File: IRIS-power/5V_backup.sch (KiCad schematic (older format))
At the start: 20 parts, among them Q61 IRLML6402, U61 LTC3110, U62 PCA9537

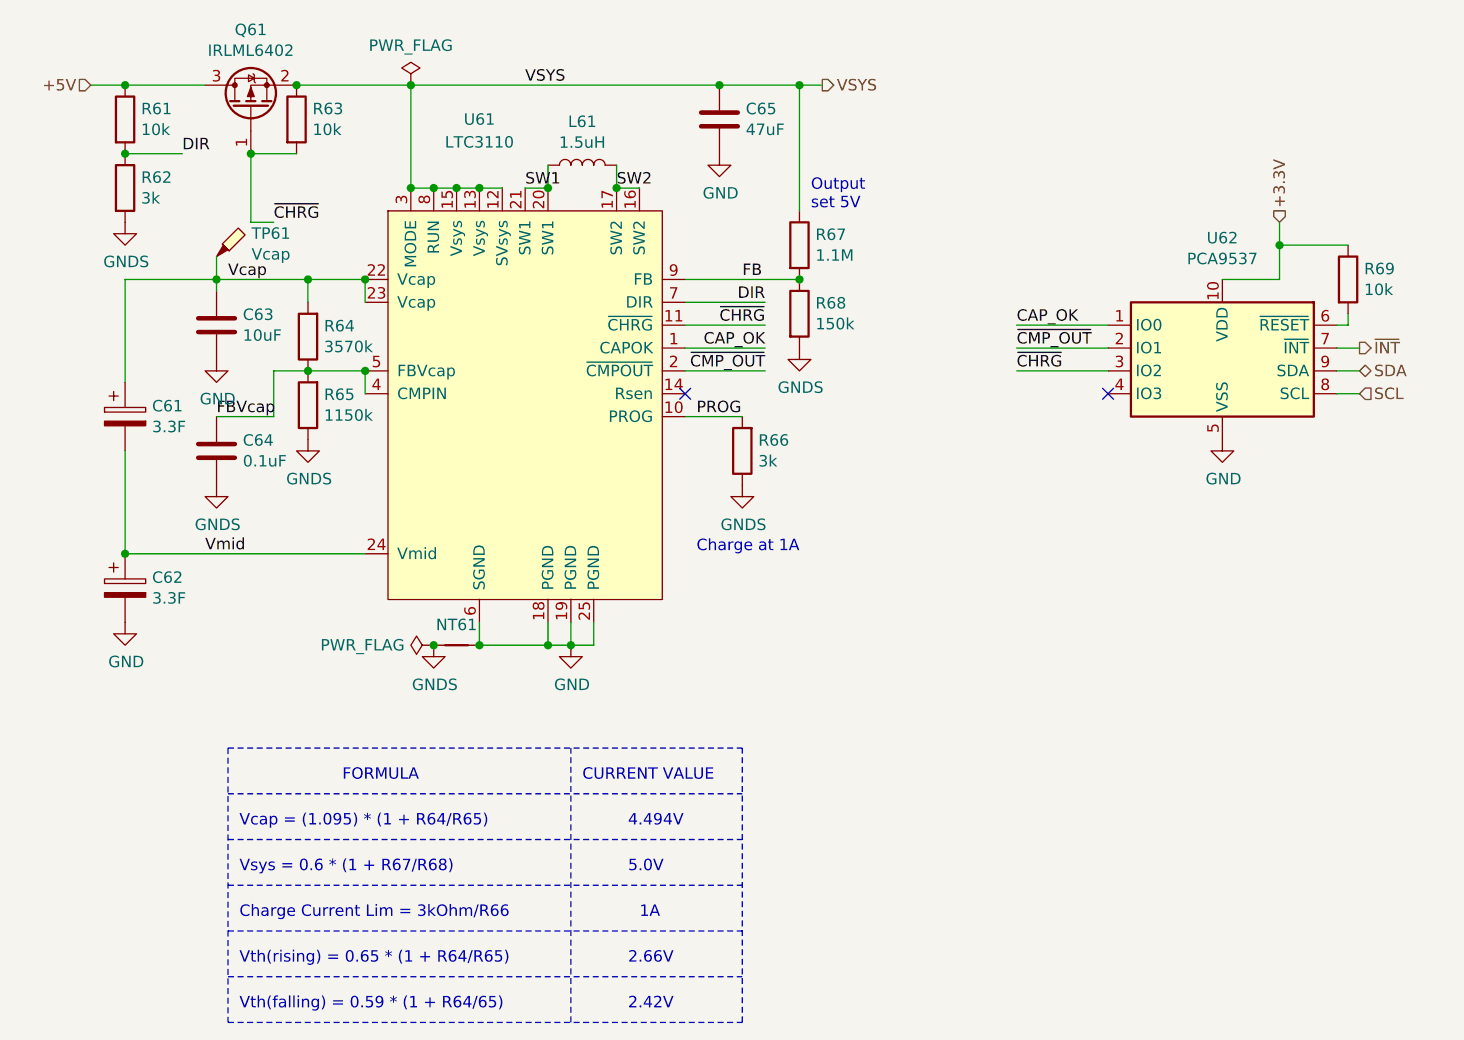
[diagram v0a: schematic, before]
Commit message: Adjusted silkscreen
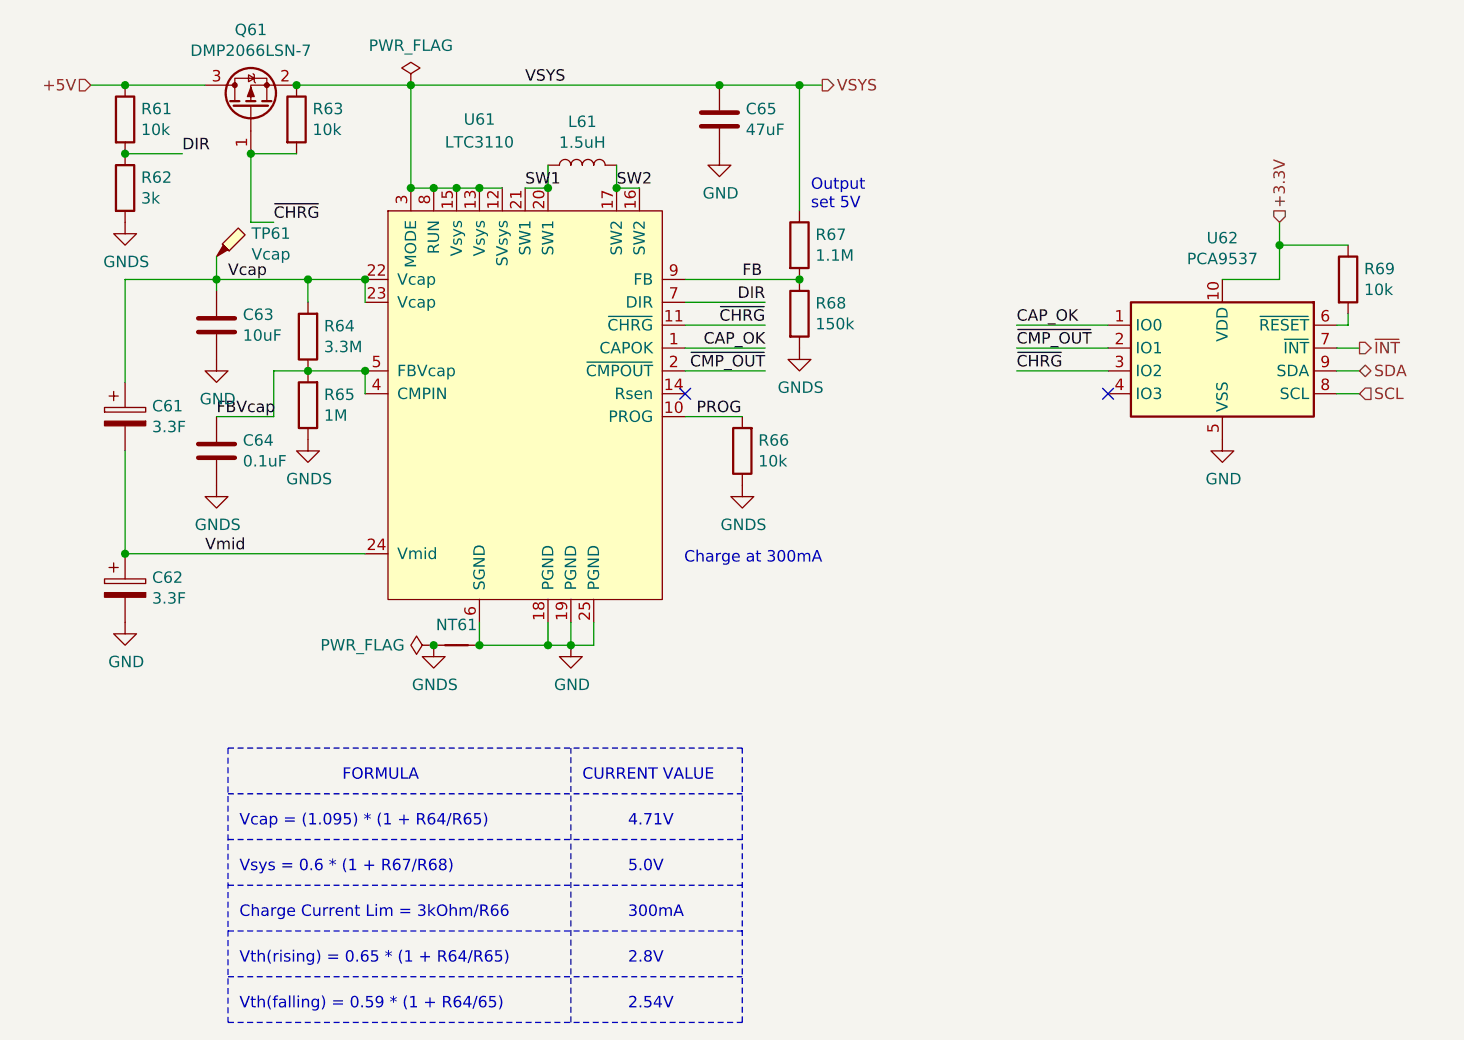
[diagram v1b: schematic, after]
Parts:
- Q61: value IRLML6402 -> DMP2066LSN-7; Digikey PN (none) -> DMP2066LSNDICT-ND
- R62: Digikey PN (none) -> RMCF0603FT3K00CT-ND
- R64: value 3570k -> 3.3M; Digikey PN (none) -> RMCF0603FT3M30CT-ND
- R65: value 1150k -> 1M; Digikey PN (none) -> RMCF0603FG1M00CT-ND
- R66: value 3k -> 10k; Digikey PN (none) -> RMCF0603FT3K00CT-ND
- R67: Digikey PN (none) -> 541-1.10MHCT-ND
- R68: Digikey PN (none) -> 311-150KHRCT-ND
- TP61: Digikey PN (none) -> 36-5006-ND
- U62: Digikey PN (none) -> 568-1837-1-ND
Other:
- note added: "2.54V"
- note added: "2.8V"
- note added: "300mA"
- note added: "4.71V"
- note added: "Charge at 300mA\n"
- note removed: "1A"
- note removed: "2.42V"
- note removed: "2.66V"
- note removed: "4.494V"
- note removed: "Charge at 1A"
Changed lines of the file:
@@
 F 2 "Resistor_SMD:R_0603_1608Metric" V 5580 3500 50  0001 C CNN
 F 3 "~" H 5650 3500 50  0001 C CNN
+F 4 "541-1.10MHCT-ND" H 5650 3500 50  0001 C CNN "Digikey PN"
 	1    5650 3500
 	1    0    0    -1
@@
 F 2 "Resistor_SMD:R_0603_1608Metric" V 5580 3800 50  0001 C CNN
 F 3 "~" H 5650 3800 50  0001 C CNN
+F 4 "311-150KHRCT-ND" H 5650 3800 50  0001 C CNN "Digikey PN"
 	1    5650 3800
 	1    0    0    -1
@@
 	1    0    0    -1
 $EndComp
-Text Notes 5650 4850 2    50   ~ 0
-Charge at 1A
+Text Notes 5750 4900 2    50   ~ 0
+Charge at 300mA\n
 Text Notes 5700 3350 0    50   ~ 0
 Output\nset 5V
@@
 F 2 "Resistor_SMD:R_0603_1608Metric" V 2630 3250 50  0001 C CNN
 F 3 "~" H 2700 3250 50  0001 C CNN
+F 4 "RMCF0603FT3K00CT-ND" H 2700 3250 50  0001 C CNN "Digikey PN"
 	1    2700 3250
 	1    0    0    -1
@@
 AR Path="/5F41BCFC/5F455591" Ref="R64"  Part="1"
 F 0 "R64" H 3430 3854 50  0000 R CNN
-F 1 "3570k" H 3430 3945 50  0000 R CNN
+F 1 "3.3M" H 3430 3945 50  0000 R CNN
 F 2 "Resistor_SMD:R_0603_1608Metric" V 3430 3900 50  0001 C CNN
 F 3 "~" H 3500 3900 50  0001 C CNN
+F 4 "RMCF0603FT3M30CT-ND" H 3500 3900 50  0001 C CNN "Digikey PN"
 	1    3500 3900
 	-1   0    0    1
@@
 AR Path="/5F41BCFC/5F455597" Ref="R65"  Part="1"
 F 0 "R65" H 3430 4154 50  0000 R CNN
-F 1 "1150k" H 3430 4245 50  0000 R CNN
+F 1 "1M" H 3430 4245 50  0000 R CNN
 F 2 "Resistor_SMD:R_0603_1608Metric" V 3430 4200 50  0001 C CNN
 F 3 "~" H 3500 4200 50  0001 C CNN
+F 4 "RMCF0603FG1M00CT-ND" H 3500 4200 50  0001 C CNN "Digikey PN"
 	1    3500 4200
 	-1   0    0    1
@@
 AR Path="/5F41BCFC/5F45559D" Ref="R66"  Part="1"
 F 0 "R66" H 5330 4354 50  0000 R CNN
-F 1 "3k" H 5330 4445 50  0000 R CNN
+F 1 "10k" H 5330 4445 50  0000 R CNN
 F 2 "Resistor_SMD:R_0603_1608Metric" V 5330 4400 50  0001 C CNN
 F 3 "~" H 5400 4400 50  0001 C CNN
+F 4 "RMCF0603FT3K00CT-ND" H 5400 4400 50  0001 C CNN "Digikey PN"
 	1    5400 4400
 	-1   0    0    1
@@
 AR Path="/5F41BCFC/5F4555F0" Ref="Q61"  Part="1"
 F 0 "Q61" V 3592 2900 50  0000 C CNN
-F 1 "IRLML6402" V 3501 2900 50  0000 C CNN
+F 1 "DMP2066LSN-7" V 3501 2900 50  0000 C CNN
 F 2 "Package_TO_SOT_SMD:SOT-23" H 3450 2825 50  0001 L CIN
-F 3 "https://www.infineon.com/dgdl/irlml6402pbf.pdf?fileId=5546d462533600a401535668d5c2263c" H 3250 2900 50  0001 L CNN
+F 3 "~" H 3250 2900 50  0001 L CNN
+F 4 "DMP2066LSNDICT-ND" H 3250 2900 50  0001 C CNN "Digikey PN"
 	1    3250 2900
 	0    -1   -1   0
@@
 F 2 "Package_SO:TSSOP-10_3x3mm_P0.5mm" H 8500 3600 50  0001 C CNN
 F 3 "https://www.nxp.com/docs/en/data-sheet/PCA9537.pdf" H 7300 2250 50  0001 C CNN
+F 4 "568-1837-1-ND" H 7500 3950 50  0001 C CNN "Digikey PN"
 	1    7500 3950
 	-1   0    0    -1
@@
 F 2 "TestPoint:TestPoint_Keystone_5000-5004_Miniature" H 3300 3550 50  0001 C CNN
 F 3 "~" H 3300 3550 50  0001 C CNN
+F 4 "36-5006-ND" H 3100 3550 50  0001 C CNN "Digikey PN"
 	1    3100 3550
 	1    0    0    -1
@@
 	3150 6100 5400 6100
 Text Notes 4900 6050 0    50   ~ 0
-4.494V
+4.71V
 Wire Notes Line
 	3150 6300 5400 6300
@@
 Text Notes 3200 6450 0    50   ~ 0
 Charge Current Lim = 3kOhm/R66
-Text Notes 4950 6450 0    50   ~ 0
-1A
+Text Notes 4900 6450 0    50   ~ 0
+300mA
 Text Notes 3200 6650 0    50   ~ 0
 Vth(rising) = 0.65 * (1 + R64/R65)
@@
 Vth(falling) = 0.59 * (1 + R64/65)
 Text Notes 4900 6650 0    50   ~ 0
-2.66V
+2.8V
 Text Notes 4900 6850 0    50   ~ 0
-2.42V
+2.54V
 Wire Notes Line
 	4650 6900 4650 5700

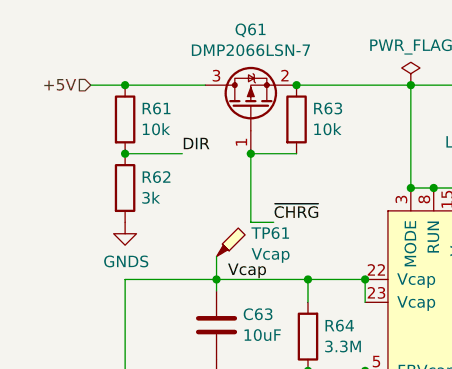
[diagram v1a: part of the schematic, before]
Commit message: USB C power prototype
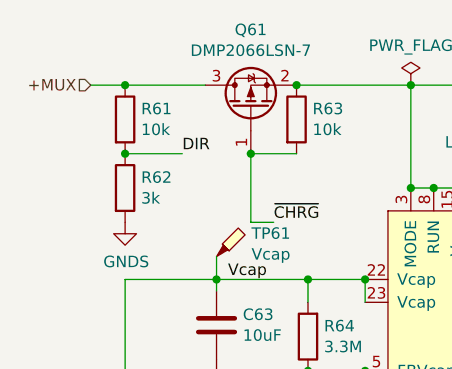
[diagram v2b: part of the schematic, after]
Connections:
- net +5V renamed +MUX
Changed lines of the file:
@@
 $Descr A4 11693 8268
 encoding utf-8
-Sheet 6 8
+Sheet 6 9
 Title ""
 Date ""
@@
 Connection ~ 2700 3100
 Text HLabel 2550 2800 0    50   Input ~ 0
-+5V
++MUX
 Text HLabel 5750 2800 2    50   Output ~ 0
 VSYS

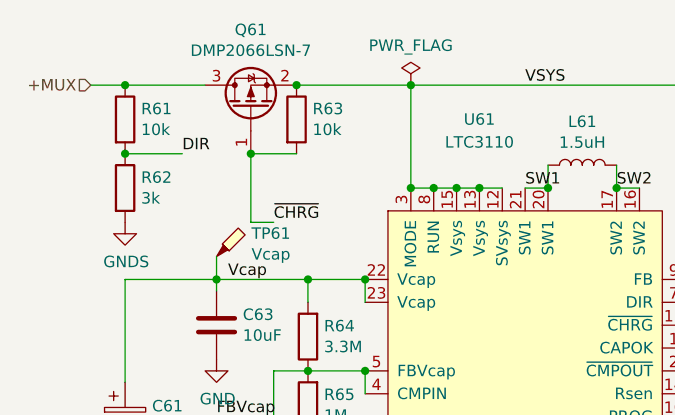
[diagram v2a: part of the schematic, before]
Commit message: Updated HV supply
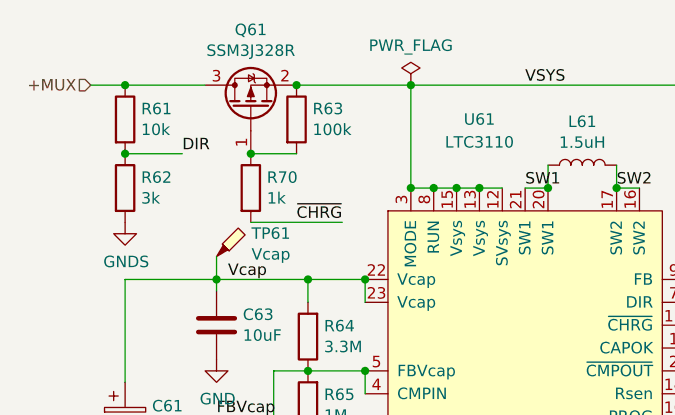
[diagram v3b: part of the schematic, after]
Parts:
- removed Q61: DMP2066LSN-7, Package_TO_SOT_SMD:SOT-23, symbol Transistor_FET:IRLML6402
- added Q61: SSM3J328R, Package_TO_SOT_SMD:SOT-23, symbol Device:Q_PMOS_GSD
- added R70: 1k, Resistor_SMD:R_0603_1608Metric, symbol Device:R
- R63: value 10k -> 100k
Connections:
- net +MUX: now also Q61.3 (D)
- net VSYS: now also Q61.2 (S)
- net ~CHRG: now also R70.2; no longer R63.2
- new net: Q61.1 (G), R63.2, R70.1
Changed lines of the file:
@@
 	1    0    0    -1
 $EndComp
-Connection ~ 3450 2800
 $Comp
 L Device:CP C?
@@
 	1    0    0    -1
 $EndComp
-$Comp
-L Transistor_FET:IRLML6402 Q?
-U 1 1 5F4555F0
-P 3250 2900
-AR Path="/5F4555F0" Ref="Q?"  Part="1"
-AR Path="/5F41BCFC/5F4555F0" Ref="Q61"  Part="1"
-F 0 "Q61" V 3592 2900 50  0000 C CNN
-F 1 "DMP2066LSN-7" V 3501 2900 50  0000 C CNN
-F 2 "Package_TO_SOT_SMD:SOT-23" H 3450 2825 50  0001 L CIN
-F 3 "~" H 3250 2900 50  0001 L CNN
-F 4 "DMP2066LSNDICT-ND" H 3250 2900 50  0001 C CNN "Digikey PN"
-	1    3250 2900
-	0    -1   -1   0
-$EndComp
-Wire Wire Line
-	3250 3100 3250 3400
-Connection ~ 3250 3100
 Wire Wire Line
 	3050 2800 2700 2800
@@
 AR Path="/5F41BCFC/5F4555FC" Ref="R63"  Part="1"
 F 0 "R63" H 3520 2996 50  0000 L CNN
-F 1 "10k" H 3520 2905 50  0000 L CNN
+F 1 "100k" H 3520 2905 50  0000 L CNN
 F 2 "Resistor_SMD:R_0603_1608Metric" V 3380 2950 50  0001 C CNN
 F 3 "~" H 3450 2950 50  0001 C CNN
@@
 	3950 2800 5300 2800
 Wire Wire Line
-	3350 3400 3250 3400
-Wire Wire Line
 	2950 3100 2700 3100
 Connection ~ 2700 3100
@@
 Text Label 2950 3100 0    50   ~ 0
 DIR
-Text Label 3350 3400 0    50   ~ 0
+Text Label 3650 3400 2    50   ~ 0
 ~CHRG
 NoConn ~ 7000 4150
@@
 Wire Notes Line
 	3150 5700 5400 5700
+$Comp
+L Device:Q_PMOS_GSD Q61
+U 1 1 5FAD0F29
+P 3250 2900
+F 0 "Q61" V 3592 2900 50  0000 C CNN
+F 1 "SSM3J328R" V 3501 2900 50  0000 C CNN
+F 2 "Package_TO_SOT_SMD:SOT-23" H 3450 3000 50  0001 C CNN
+F 3 "~" H 3250 2900 50  0001 C CNN
+	1    3250 2900
+	0    -1   -1   0
+$EndComp
+Connection ~ 3450 2800
+$Comp
+L Device:R R70
+U 1 1 5FAD3E6D
+P 3250 3250
+F 0 "R70" H 3320 3296 50  0000 L CNN
+F 1 "1k" H 3320 3205 50  0000 L CNN
+F 2 "Resistor_SMD:R_0603_1608Metric" V 3180 3250 50  0001 C CNN
+F 3 "~" H 3250 3250 50  0001 C CNN
+	1    3250 3250
+	1    0    0    -1
+$EndComp
+Connection ~ 3250 3100
+Wire Wire Line
+	3250 3400 3650 3400
 $EndSCHEMATC

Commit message: Updated to V4.01
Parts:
- Q61: Digikey PN (none) -> SSM3J328RLFCT-ND
- R63: Digikey PN RNCP0603FTD10K0CT-ND -> RR08P100KDCT-ND
- R66: Digikey PN RMCF0603FT3K00CT-ND -> RNCP0603FTD10K0CT-ND
- R70: Digikey PN (none) -> RMCF0603FT1K00CT-ND
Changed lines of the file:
@@
 F 2 "Resistor_SMD:R_0603_1608Metric" V 5330 4400 50  0001 C CNN
 F 3 "~" H 5400 4400 50  0001 C CNN
-F 4 "RMCF0603FT3K00CT-ND" H 5400 4400 50  0001 C CNN "Digikey PN"
+F 4 "RNCP0603FTD10K0CT-ND" H 5400 4400 50  0001 C CNN "Digikey PN"
 	1    5400 4400
 	-1   0    0    1
@@
 F 2 "Resistor_SMD:R_0603_1608Metric" V 3380 2950 50  0001 C CNN
 F 3 "~" H 3450 2950 50  0001 C CNN
-F 4 "RNCP0603FTD10K0CT-ND" H 3450 2950 50  0001 C CNN "Digikey PN"
+F 4 "RR08P100KDCT-ND" H 3450 2950 50  0001 C CNN "Digikey PN"
 	1    3450 2950
 	1    0    0    -1
@@
 F 2 "Package_TO_SOT_SMD:SOT-23" H 3450 3000 50  0001 C CNN
 F 3 "~" H 3250 2900 50  0001 C CNN
+F 4 "SSM3J328RLFCT-ND" H 3250 2900 50  0001 C CNN "Digikey PN"
 	1    3250 2900
 	0    -1   -1   0
@@
 F 2 "Resistor_SMD:R_0603_1608Metric" V 3180 3250 50  0001 C CNN
 F 3 "~" H 3250 3250 50  0001 C CNN
+F 4 "RMCF0603FT1K00CT-ND" H 3250 3250 50  0001 C CNN "Digikey PN"
 	1    3250 3250
 	1    0    0    -1
